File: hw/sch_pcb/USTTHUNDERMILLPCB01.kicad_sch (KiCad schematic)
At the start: 12 parts, among them J2 SM03B-GHS-TB, U1 ISL21080DIH312Z-TK 1V25, U2 OPA314

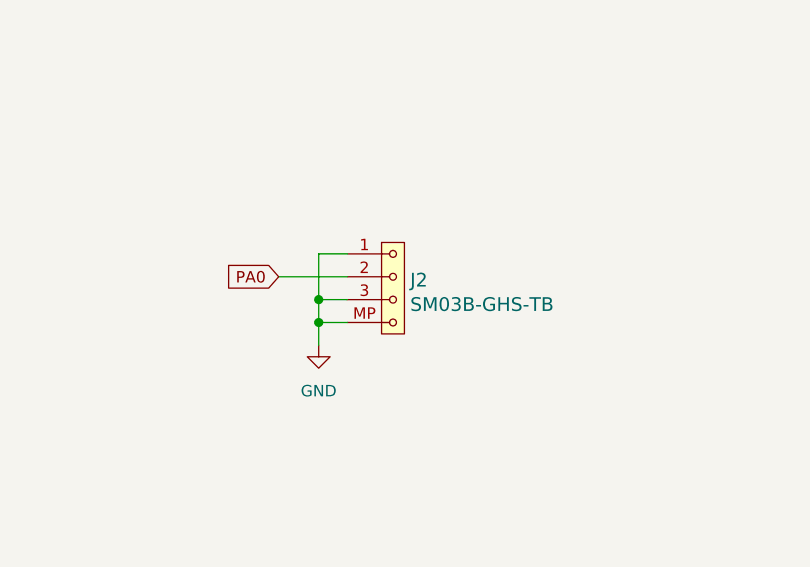
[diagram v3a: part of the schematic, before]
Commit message: updates of schematics and layout: solve: #6, #3, #8, #10
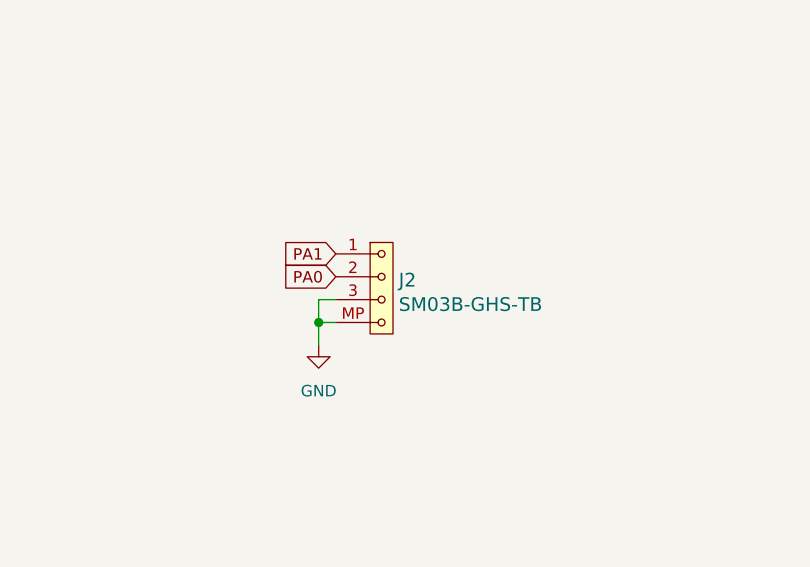
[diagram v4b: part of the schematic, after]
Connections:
- net GND: no longer J2.1
- net PA1: now also J2.1
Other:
- moved on the sheet: J2
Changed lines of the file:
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@@
   (junction (at 127.635 124.46) (diameter 1.016) (color 0 0 0 0)
   )
-  (junction (at 219.075 86.36) (diameter 1.016) (color 0 0 0 0)
-  )
   (wire (pts (xy 149.86 85.09) (xy 167.64 85.09))
     (stroke (width 0) (type solid) (color 0 0 0 0))
@@
     (stroke (width 0) (type solid) (color 0 0 0 0))
   )
-  (wire (pts (xy 219.075 81.28) (xy 219.075 86.36))
-    (stroke (width 0) (type solid) (color 0 0 0 0))
-  )
   (wire (pts (xy 219.075 86.36) (xy 219.075 88.9))
     (stroke (width 0) (type solid) (color 0 0 0 0))
@@
     (stroke (width 0) (type solid) (color 0 0 0 0))
   )
-  (wire (pts (xy 222.25 81.28) (xy 219.075 81.28))
-    (stroke (width 0) (type solid) (color 0 0 0 0))
-  )
   (wire (pts (xy 36.83 29.21) (xy 39.37 29.21))
     (stroke (width 0) (type solid) (color 0 0 0 0))
@@
     (stroke (width 0) (type solid) (color 0 0 0 0))
   )
-  (wire (pts (xy 214.63 83.82) (xy 222.25 83.82))
-    (stroke (width 0) (type solid) (color 0 0 0 0))
-  )
   (wire (pts (xy 127.635 106.68) (xy 135.255 106.68))
     (stroke (width 0) (type solid) (color 0 0 0 0))
@@
     (stroke (width 0) (type solid) (color 0 0 0 0))
   )
-  (wire (pts (xy 219.075 88.9) (xy 222.25 88.9))
+  (wire (pts (xy 219.075 88.9) (xy 220.98 88.9))
     (stroke (width 0) (type solid) (color 0 0 0 0))
   )
@@
     (stroke (width 0) (type solid) (color 0 0 0 0))
   )
-  (wire (pts (xy 219.075 86.36) (xy 222.25 86.36))
+  (wire (pts (xy 219.075 86.36) (xy 220.98 86.36))
     (stroke (width 0) (type solid) (color 0 0 0 0))
   )
@@
   (label "REF_1V25" (at 39.37 29.21 0)
     (effects (font (size 1.524 1.524)) (justify left bottom))
+  )
+  (global_label "PA1" (shape input) (at 220.98 81.28 180) (fields_autoplaced)
+    (effects (font (size 1.27 1.27)) (justify right))
+    (property "Intersheet References" "${INTERSHEET_REFS}" (id 0) (at 214.9988 81.3594 0)
+      (effects (font (size 1.27 1.27)) (justify right) hide)
+    )
   )
   (global_label "ROTOR_GND" (shape input) (at 85.09 88.265 180) (fields_autoplaced)
@@
     )
   )
-  (global_label "PA0" (shape input) (at 214.63 83.82 180) (fields_autoplaced)
+  (global_label "PA0" (shape input) (at 220.98 83.82 180) (fields_autoplaced)
     (effects (font (size 1.27 1.27)) (justify right))
-    (property "Intersheet References" "${INTERSHEET_REFS}" (id 0) (at 208.6488 83.8994 0)
+    (property "Intersheet References" "${INTERSHEET_REFS}" (id 0) (at 214.9988 83.8994 0)
       (effects (font (size 1.27 1.27)) (justify right) hide)
     )
@@
     (pin "2")
   )
-  (symbol (lib_id "MLAB_CONNECTORS_JST:SM03B-GHS-TB") (at 227.33 85.09 0) (unit 1)
-    (in_bom yes) (on_board yes) (fields_autoplaced)
-    (property "Reference" "J2" (id 0) (at 229.2351 84.2024 0)
+  (symbol (lib_id "MLAB_CONNECTORS_JST:SM03B-GHS-TB") (at 226.06 85.09 0) (unit 1)
+    (in_bom yes) (on_board yes) (fields_autoplaced)
+    (property "Reference" "J2" (id 0) (at 227.9651 84.2024 0)
       (effects (font (size 1.524 1.524)) (justify left))
     )
-    (property "Value" "SM03B-GHS-TB" (id 1) (at 229.2351 86.91 0)
+    (property "Value" "SM03B-GHS-TB" (id 1) (at 227.9651 86.91 0)
       (effects (font (size 1.524 1.524)) (justify left))
     )
-    (property "Footprint" "Connector_JST:JST_GH_SM03B-GHS-TB_1x03-1MP_P1.25mm_Horizontal" (id 2) (at 229.2351 88.2638 0)
+    (property "Footprint" "Connector_JST:JST_GH_SM03B-GHS-TB_1x03-1MP_P1.25mm_Horizontal" (id 2) (at 227.9651 88.2638 0)
       (effects (font (size 1.524 1.524)) (justify left) hide)
     )
-    (property "Datasheet" "" (id 3) (at 227.33 81.28 0)
+    (property "Datasheet" "" (id 3) (at 226.06 81.28 0)
       (effects (font (size 1.524 1.524)))
     )
-    (property "UST_ID" "612880e51287500165a978de" (id 4) (at 227.33 85.09 0)
+    (property "UST_ID" "612880e51287500165a978de" (id 4) (at 226.06 85.09 0)
       (effects (font (size 1.27 1.27)) hide)
     )
@@
     )
     (path "/f1d72f98-8869-41cc-b10e-5c93f9725bfa/72988fb4-fc5c-4523-9e3f-28b1ee7a0732"
-      (reference "C25") (unit 1) (value "4u7") (footprint "")
+      (reference "C25") (unit 1) (value "4u7") (footprint "Capacitor_SMD:C_0603_1608Metric")
     )
     (path "/63710ae2-0173-429f-930e-1f82ffa3907c"
@@
       (reference "D6") (unit 1) (value "RED") (footprint "LED_SMD:LED_0603_1608Metric")
     )
+    (path "/c65d3f2e-8a0d-4ec9-900d-154ccfd9e32b/ad0a10ac-8393-48a8-ba42-109c83d5dc51"
+      (reference "F1") (unit 1) (value "350mA") (footprint "Fuse:Fuse_1812_4532Metric")
+    )
     (path "/f1d72f98-8869-41cc-b10e-5c93f9725bfa/31c3b6c0-9e01-4fba-84eb-0a4818260865"
       (reference "J1") (unit 1) (value "SM06B-GHS-TB") (footprint "Connector_JST:JST_GH_SM06B-GHS-TB_1x06-1MP_P1.25mm_Horizontal")
@@
     )
     (path "/f1d72f98-8869-41cc-b10e-5c93f9725bfa/759badb8-78f9-41f6-99f7-9e1a669adf06"
-      (reference "JP1") (unit 1) (value "SolderJumper_2_Bridged") (footprint "")
+      (reference "JP1") (unit 1) (value "SolderJumper_2_Bridged") (footprint "Jumper:SolderJumper-2_P1.3mm_Bridged_RoundedPad1.0x1.5mm")
     )
     (path "/f1d72f98-8869-41cc-b10e-5c93f9725bfa/554e3832-2a3b-426c-976b-3a4363c7d71c"
-      (reference "JP2") (unit 1) (value "SolderJumper_2_Open") (footprint "")
+      (reference "JP2") (unit 1) (value "SolderJumper_2_Open") (footprint "Jumper:SolderJumper-2_P1.3mm_Open_RoundedPad1.0x1.5mm")
     )
     (path "/f1d72f98-8869-41cc-b10e-5c93f9725bfa/eb62ae2e-c38d-462a-8b75-793a619cd9be"
-      (reference "JP3") (unit 1) (value "SolderJumper_2_Open") (footprint "")
+      (reference "JP3") (unit 1) (value "SolderJumper_2_Open") (footprint "Jumper:SolderJumper-2_P1.3mm_Open_RoundedPad1.0x1.5mm")
     )
     (path "/f1d72f98-8869-41cc-b10e-5c93f9725bfa/fefffef2-b902-4577-8ac1-b36192c7493b"
@@
     )
     (path "/f1d72f98-8869-41cc-b10e-5c93f9725bfa/95e5c7d9-5157-4e26-b347-7afccfecbda5"
-      (reference "R26") (unit 1) (value "33R") (footprint "")
+      (reference "R26") (unit 1) (value "33R") (footprint "Resistor_SMD:R_0603_1608Metric")
     )
     (path "/f1d72f98-8869-41cc-b10e-5c93f9725bfa/a4fcada3-4f52-46a5-ac5b-6f841abab351"

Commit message: analogue power
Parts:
- added JP4: Jumper_2_Bridged, NetTie:NetTie-2_SMD_Pad0.5mm, symbol Device:NetTie_2
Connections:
- net GND: now also JP4.1; no longer C1.2, C3.1, C5.1, D1.2 (A2), J2.3, J2.MP, U1.3 (GND), U2.2 (V-)
- new net GNDA: C1.2, C3.1, C5.1, D1.2 (A2), J2.3, J2.MP, JP4.2, U1.3 (GND), U2.2 (V-)
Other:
- moved on the sheet: C2, C3, C4, C5, D1, J2, R1, R2, R3, U2

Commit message: Update layout
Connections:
- net +3.3VP renamed +3.3VA
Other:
- moved on the sheet: C5, JP4
